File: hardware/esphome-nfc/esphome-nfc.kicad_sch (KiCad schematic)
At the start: 12 parts, among them J1 USB_C_Receptacle_USB2.0_14P, U1 ESP32-C3-WROOM-02, U2 PN7160A1HN/C100Y

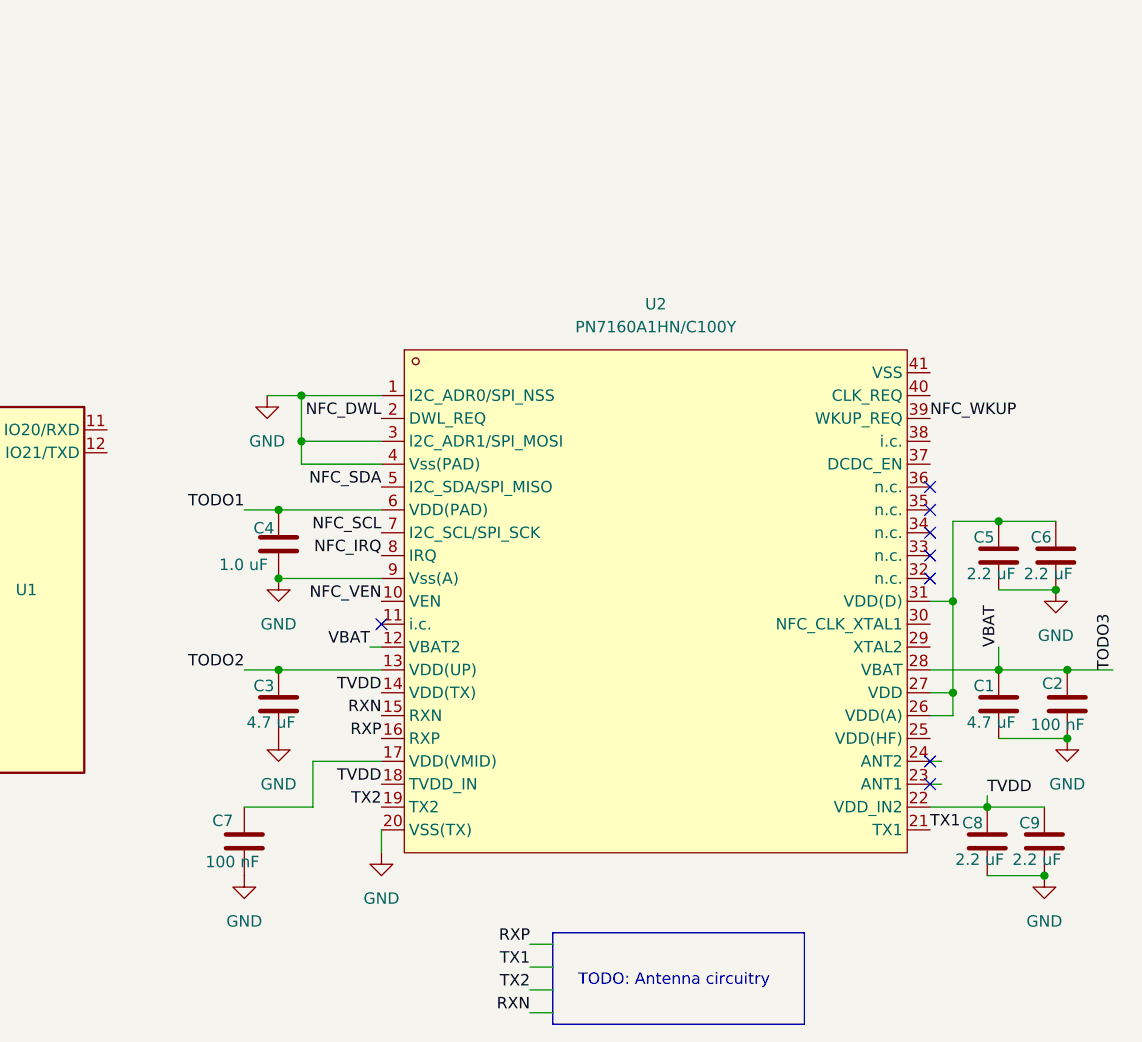
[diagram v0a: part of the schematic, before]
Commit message: Work in progress on esphome-nfc board
* Done power and clock circuit for PN7160
* Drafted the board dimensions
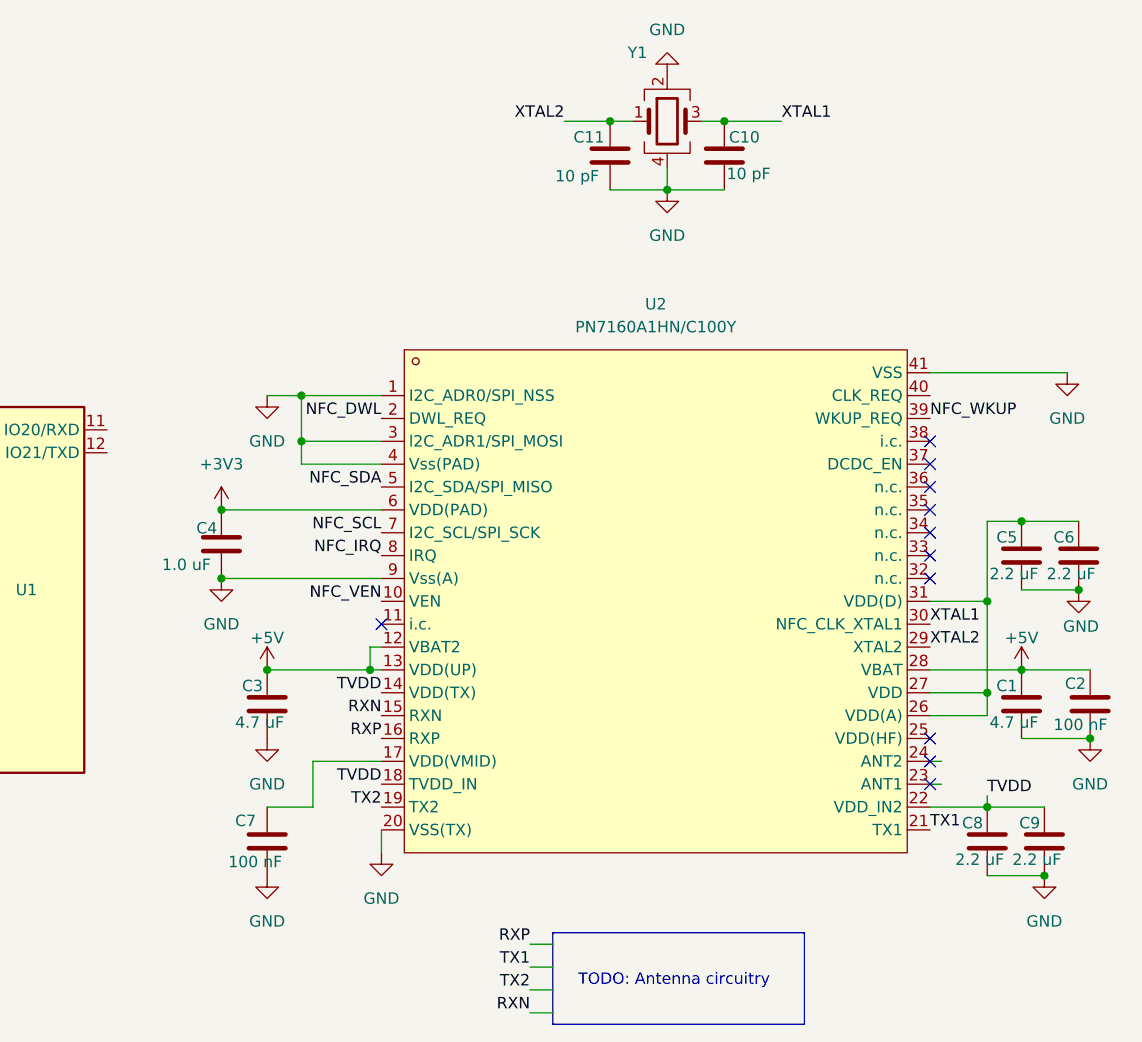
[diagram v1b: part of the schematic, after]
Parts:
- added C10, C11: 10 pF, Capacitor_SMD:C_0402_1005Metric, symbol Ostranna:10 pF
- added Y1: Crystal_GND24, Crystal:Crystal_SMD_2016-4Pin_2.0x1.6mm, symbol Device:Crystal_GND24
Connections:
- net TODO1 is gone; now on net +3V3: C4.1, U2.6 (VDD(PAD))
- net TODO3 is gone; now on net +5V: C1.1, C2.1, U2.12 (VBAT2), U2.28 (VBAT)
- net GND: now also U2.41 (VSS), C10.2, C11.2, Y1.2, Y1.4
- net XTAL2: now reaches U2.29 (XTAL2)
- net XTAL2: now also C11.1, Y1.1
- net XTAL1: now reaches U2.30 (NFC_CLK_XTAL1)
- net XTAL1: now also C10.1, Y1.3
- net TODO2 renamed +5V
- no-connect marks 12 -> 15
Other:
- moved on the sheet: C1, C2, C3, C4, C5, C6, C7

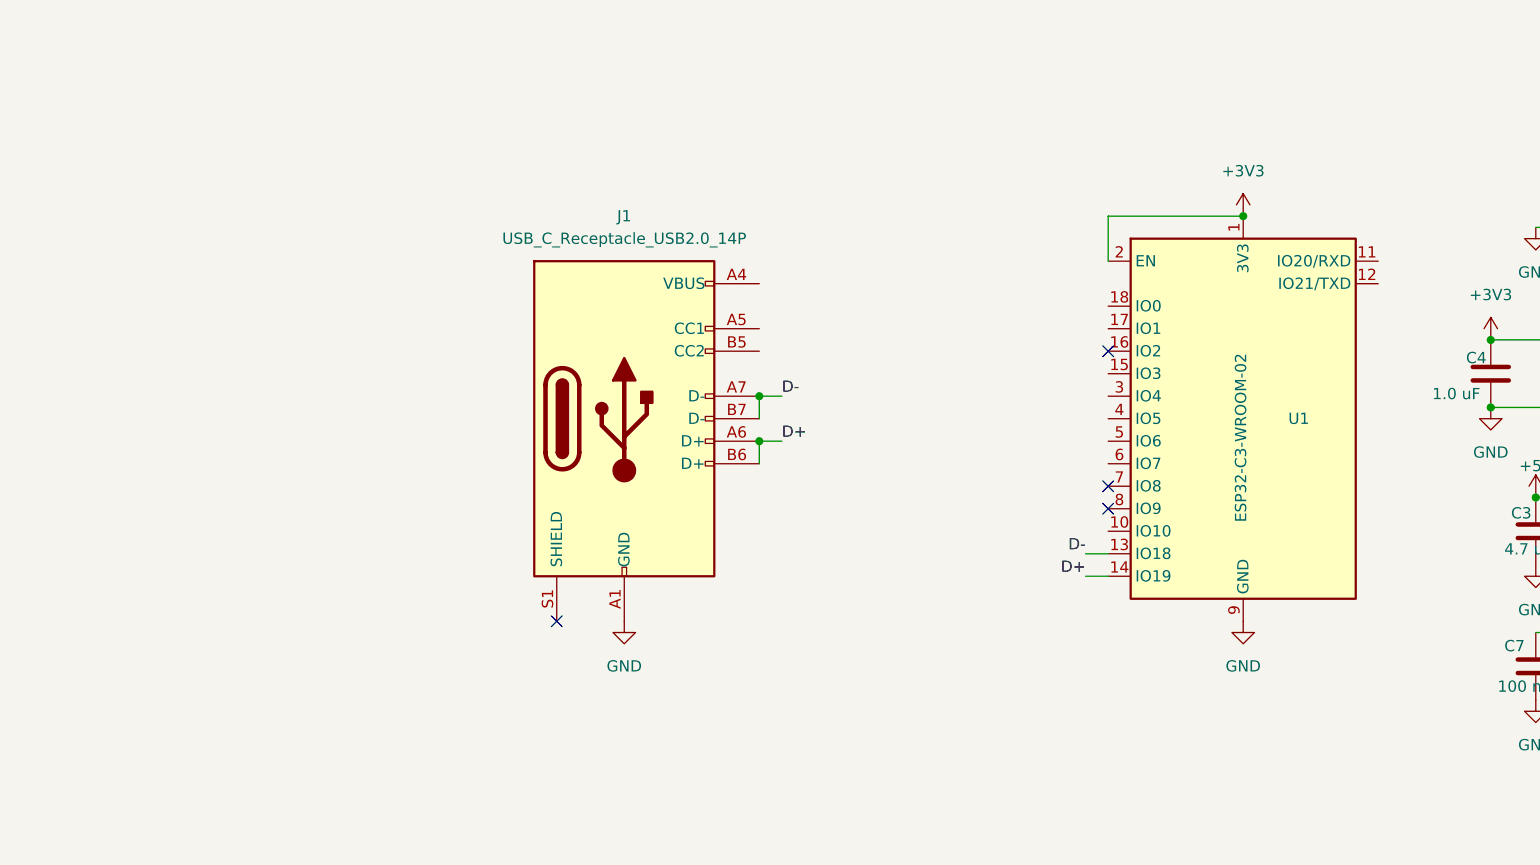
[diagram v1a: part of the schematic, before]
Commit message: Work in progress on esphome-nfc board
* Routed most of things related to the USB
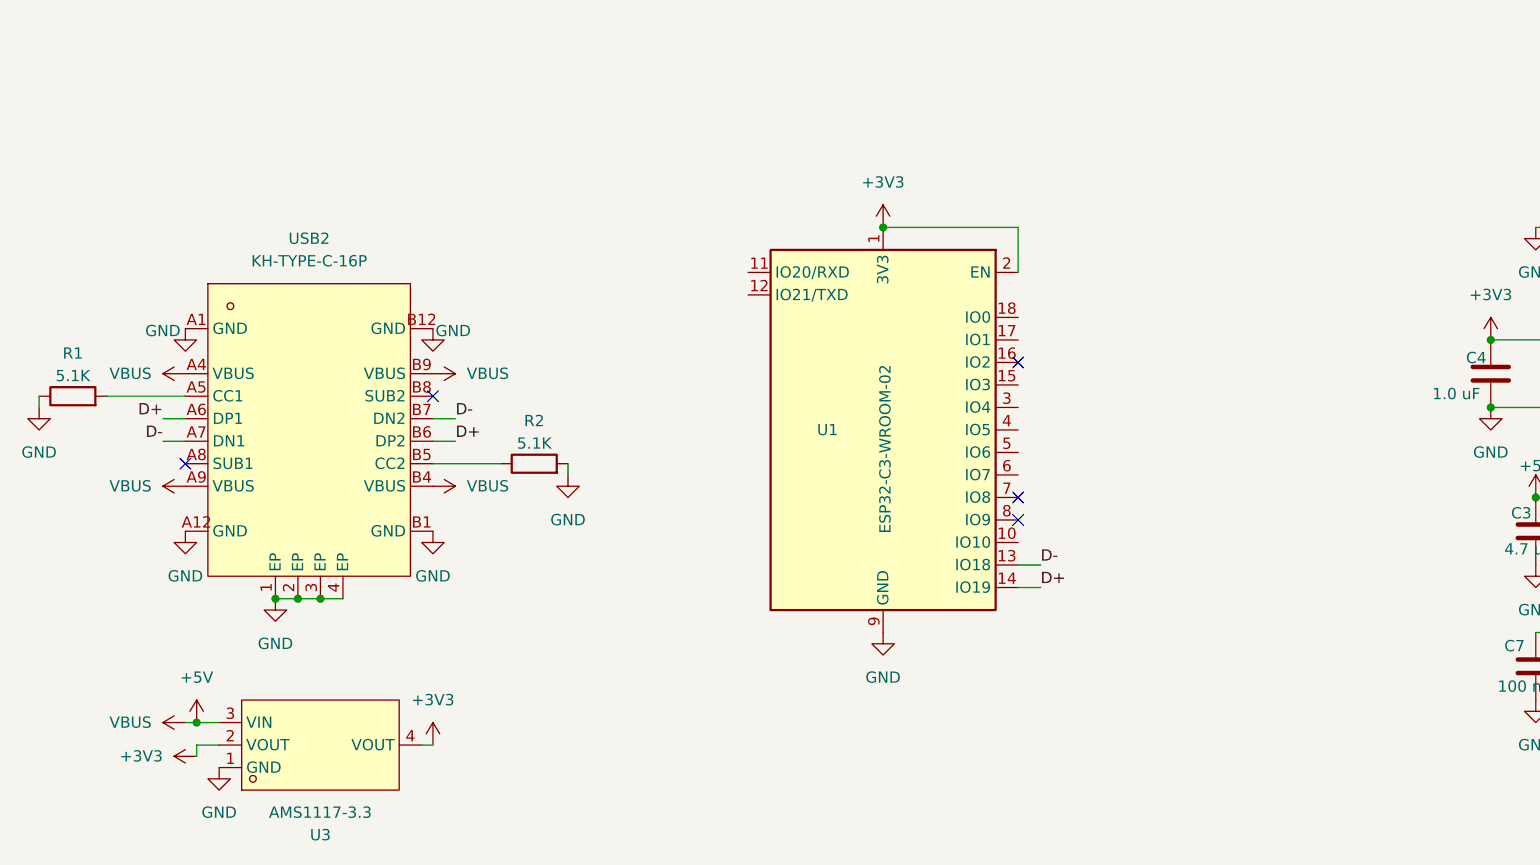
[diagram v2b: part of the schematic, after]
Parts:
- removed J1: USB_C_Receptacle_USB2.0_14P, symbol Connector:USB_C_Receptacle_USB2.0_14P
- added R1, R2: 5.1K, Resistor_SMD:R_0402_1005Metric, symbol Device:R
- added U3: AMS1117-3.3, easyeda2kicad:SOT-223-3_L6.5-W3.4-P2.30-LS7.0-BR, symbol easyeda2kicad:AMS1117-3.3
- added USB2: KH-TYPE-C-16P, easyeda2kicad:USB-C-SMD_KH-TYPE-C-16P, symbol easyeda2kicad:KH-TYPE-C-16P
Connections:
- net +3V3: now also U3.2 (VOUT), U3.4 (VOUT)
- net +5V: now also U3.3 (VIN), USB2.A4 (VBUS), USB2.A9 (VBUS), USB2.B4 (VBUS), USB2.B9 (VBUS)
- net D+: now also USB2.A6 (DP1), USB2.B6 (DP2)
- net D-: now also USB2.A7 (DN1), USB2.B7 (DN2)
- net GND: now also R1.1, R2.2, U3.1 (GND), USB2.1 (EP), USB2.2 (EP), USB2.3 (EP), USB2.4 (EP), USB2.A1 (GND), USB2.A12 (GND), USB2.B1 (GND), USB2.B12 (GND)
- new net: R2.1, USB2.B5 (CC2)
- new net: R1.2, USB2.A5 (CC1)
- no-connect marks 15 -> 16
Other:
- moved on the sheet: U1

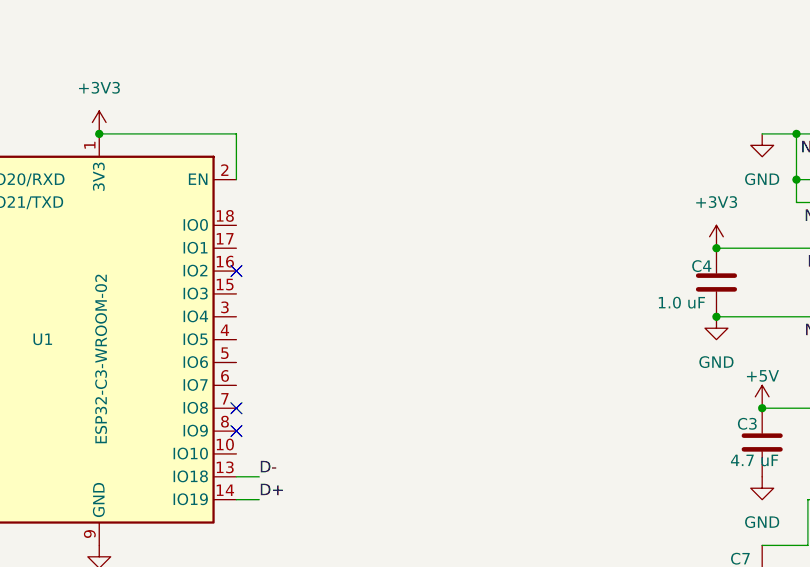
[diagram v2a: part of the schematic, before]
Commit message: Route MCU <--> NFC chip connections
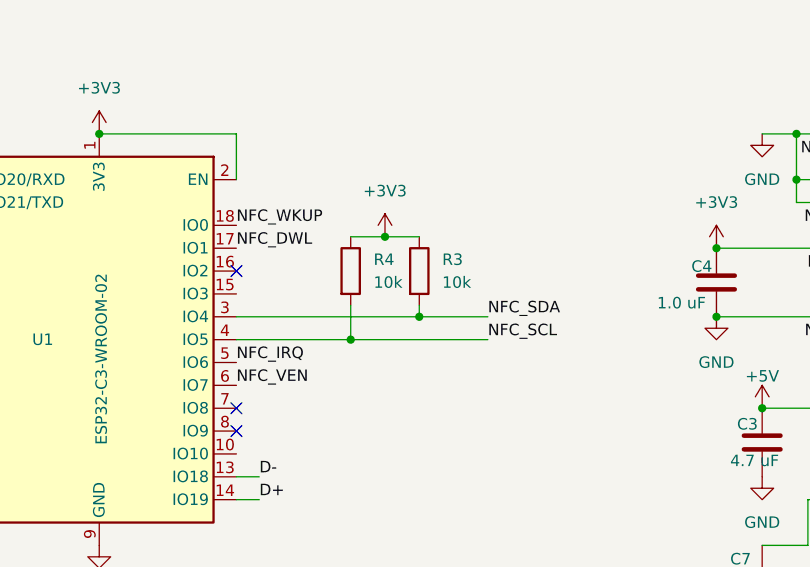
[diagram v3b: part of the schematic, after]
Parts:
- added R3, R4: 10k, Resistor_SMD:R_0402_1005Metric, symbol Ostranna:10k Resistor
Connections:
- net +3V3: now also R3.1, R4.1
- net NFC_DWL: now also U1.17 (IO1)
- net NFC_IRQ: now also U1.5 (IO6)
- net NFC_SCL: now also U1.4 (IO5), R4.2
- net NFC_SDA: now also U1.3 (IO4), R3.2
- net NFC_VEN: now also U1.6 (IO7)
- net NFC_WKUP: now also U1.18 (IO0)

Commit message: Work in progress on esphome-nfc board
* Added ESD protection chip
* Added proper LDO regulator
* Added number of testpoints to check for the potential power issues
* Added required connections for the strapping pins
* Added LED output
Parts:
- removed U3: AMS1117-3.3, easyeda2kicad:SOT-223-3_L6.5-W3.4-P2.30-LS7.0-BR, symbol easyeda2kicad:AMS1117-3.3
- added C12, C13: 1.0 uF, Capacitor_SMD:C_0603_1608Metric, symbol Ostranna:1.0 uF
- added JP1: SolderJumper_2_Open, Jumper:SolderJumper-2_P1.3mm_Open_RoundedPad1.0x1.5mm, symbol Jumper:SolderJumper_2_Open
- added LED1: 0805G (Green), easyeda2kicad:LED0805-R-RD, symbol easyeda2kicad:LED Green
- added R5, R6: 10k, Resistor_SMD:R_0402_1005Metric, symbol Ostranna:10k Resistor
- added R7: 100R, Resistor_SMD:R_0603_1608Metric, symbol Ostranna:100R Resistor
- added TP1, TP2, TP3, TP4, TP5: ~, TestPoint:TestPoint_Pad_D1.0mm, symbol Connector:TestPoint
- added U3: AP2112K-3.3TRG1, easyeda2kicad:SOT-25-5_L2.9-W1.6-P0.95-LS2.8-BL, symbol easyeda2kicad:AP2112K-3.3TRG1
- added U4: USBLC6-2P6, Package_TO_SOT_SMD:SOT-666, symbol Power_Protection:USBLC6-2P6
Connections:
- net +3V3: now also C13.1, R5.1, R6.1, R7.2, TP2.1, U3.5 (VOUT)
- net +5V: now also C12.1, TP1.1, U3.1 (VIN), U3.3 (EN), U4.5 (VBUS)
- net D+: now also U4.4 (I/O2); no longer USB2.A6 (DP1), USB2.B6 (DP2)
- net D-: now also U4.6 (I/O1); no longer USB2.A7 (DN1), USB2.B7 (DN2)
- net GND: now also C12.2, C13.2, JP1.2 (B), U3.2 (GND), U4.2 (GND); no longer USB2.1 (EP), USB2.2 (EP), USB2.3 (EP), USB2.4 (EP)
- net TVDD: now also TP3.1
- net BUZZER: now reaches U1.10 (IO10)
- net at U1.11 (IO20/RXD): now also TP5.1
- net at U1.12 (IO21/TXD): now also TP4.1
- net LED: now reaches U1.15 (IO3)
- net LED: now also LED1.2 (K)
- net at U1.16 (IO2): now also R5.2
- net at U1.7 (IO8): now also R6.2
- net at U1.8 (IO9): now also JP1.1 (A)
- new net: LED1.1 (A), R7.1
- new net DN: U4.1 (I/O1), USB2.A7 (DN1), USB2.B7 (DN2)
- new net DP: U4.3 (I/O2), USB2.A6 (DP1), USB2.B6 (DP2)
- no-connect marks 16 -> 18
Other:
- moved on the sheet: C7, R1, R2, R3, R4, USB2

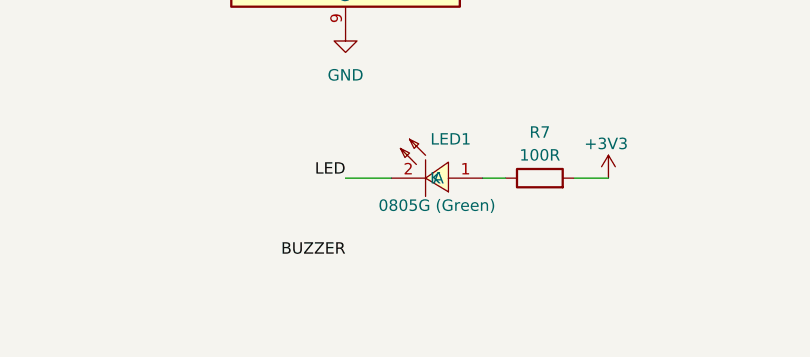
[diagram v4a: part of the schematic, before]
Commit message: esphome-nfc: route & finalize everything except for NFC antenna and corresponding matching circuit
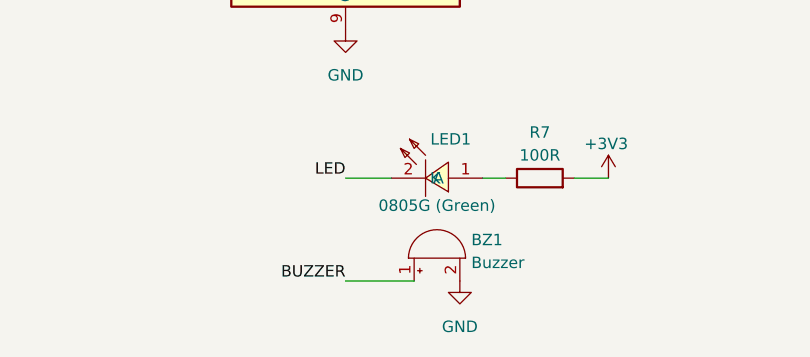
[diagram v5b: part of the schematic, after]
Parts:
- added BZ1: Buzzer, Buzzer_Beeper:Buzzer_12x9.5RM7.6, symbol Device:Buzzer
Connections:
- net BUZZER: now also BZ1.1 (+)
- net GND: now also BZ1.2 (-)
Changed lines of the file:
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@@
 	(wire
 		(pts
+			(xy 115.57 151.13) (xy 123.19 151.13)
+		)
+		(stroke
+			(width 0)
+			(type default)
+		)
+	)
+	(wire
+		(pts
 			(xy 35.56 53.34) (xy 38.1 53.34)
 		)
@@
 	)
 	(label "BUZZER"
-		(at 115.57 148.59 180)
+		(at 115.57 151.13 180)
 		(fields_autoplaced yes)
 		(effects
@@
 	)
 	(symbol
+		(lib_id "Device:Buzzer")
+		(at 125.73 148.59 90)
+		(unit 1)
+		(exclude_from_sim no)
+		(in_bom yes)
+		(on_board yes)
+		(dnp no)
+		(fields_autoplaced yes)
+		(property "Reference" "BZ1"
+			(at 129.54 146.5648 90)
+			(effects
+				(font
+					(size 1.27 1.27)
+				)
+				(justify right)
+			)
+		)
+		(property "Value" "Buzzer"
+			(at 129.54 149.1048 90)
+			(effects
+				(font
+					(size 1.27 1.27)
+				)
+				(justify right)
+			)
+		)
+		(property "Footprint" "Buzzer_Beeper:Buzzer_12x9.5RM7.6"
+			(at 123.19 149.225 90)
+			(effects
+				(font
+					(size 1.27 1.27)
+				)
+				(hide yes)
+			)
+		)
+		(property "Datasheet" "~"
+			(at 123.19 149.225 90)
+			(effects
+				(font
+					(size 1.27 1.27)
+				)
+				(hide yes)
+			)
+		)
+		(property "Description" "Buzzer, polarized"
+			(at 125.73 148.59 0)
+			(effects
+				(font
+					(size 1.27 1.27)
+				)
+				(hide yes)
+			)
+		)
+		(pin "1"
+		)
+		(pin "2"
+		)
+		(instances
+			(project ""
+				(path "/0388137f-fb41-46a6-bb35-a6e9549dd65e"
+					(reference "BZ1")
+					(unit 1)
+				)
+			)
+		)
+	)
+	(symbol
 		(lib_id "power:GND")
 		(at 233.68 54.61 0)
@@
 					(unit 1)
 				)
+			)
+		)
+	)
+	(symbol
+		(lib_id "power:GND")
+		(at 128.27 151.13 0)
+		(unit 1)
+		(exclude_from_sim no)
+		(in_bom yes)
+		(on_board yes)
+		(dnp no)
+		(property "Reference" "#PWR038"
+			(at 128.27 157.48 0)
+			(effects
+				(font
+					(size 1.27 1.27)
+				)
+				(hide yes)
+			)
+		)
+		(property "Value" "GND"
+			(at 128.27 156.21 0)
+			(effects
+				(font
+					(size 1.27 1.27)
+				)
+			)
+		)
+		(property "Footprint" ""
+			(at 128.27 151.13 0)
+			(effects
+				(font
+					(size 1.27 1.27)
+				)
+				(hide yes)
+			)
+		)
+		(property "Datasheet" ""
+			(at 128.27 151.13 0)
+			(effects
+				(font
+					(size 1.27 1.27)
+				)
+				(hide yes)
+			)
+		)
+		(property "Description" "Power symbol creates a global label with name \"GND\" , ground"
+			(at 128.27 151.13 0)
+			(effects
+				(font
+					(size 1.27 1.27)
+				)
+				(hide yes)
+			)
+		)
+		(pin "1"
+		)
+		(instances
+			(project "esphome-nfc"
+				(path "/0388137f-fb41-46a6-bb35-a6e9549dd65e"
+					(reference "#PWR038")
+					(unit 1)
+				)
